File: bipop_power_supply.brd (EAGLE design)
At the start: 160 x 100 mm, 23 parts, among them IC1 LM1117MP-3.3, IC2 LM1117MP-5.0

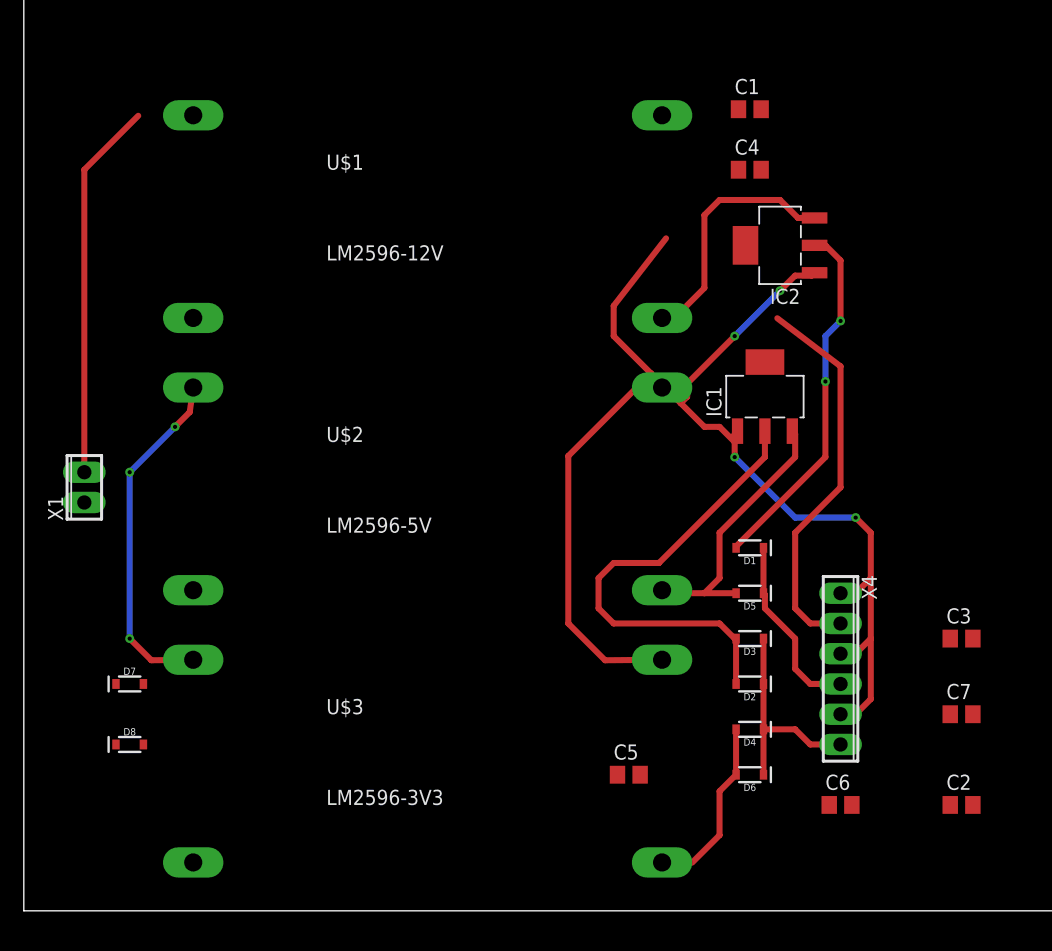
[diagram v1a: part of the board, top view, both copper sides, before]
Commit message: plytka z kondensatorami i diodami +pdfy
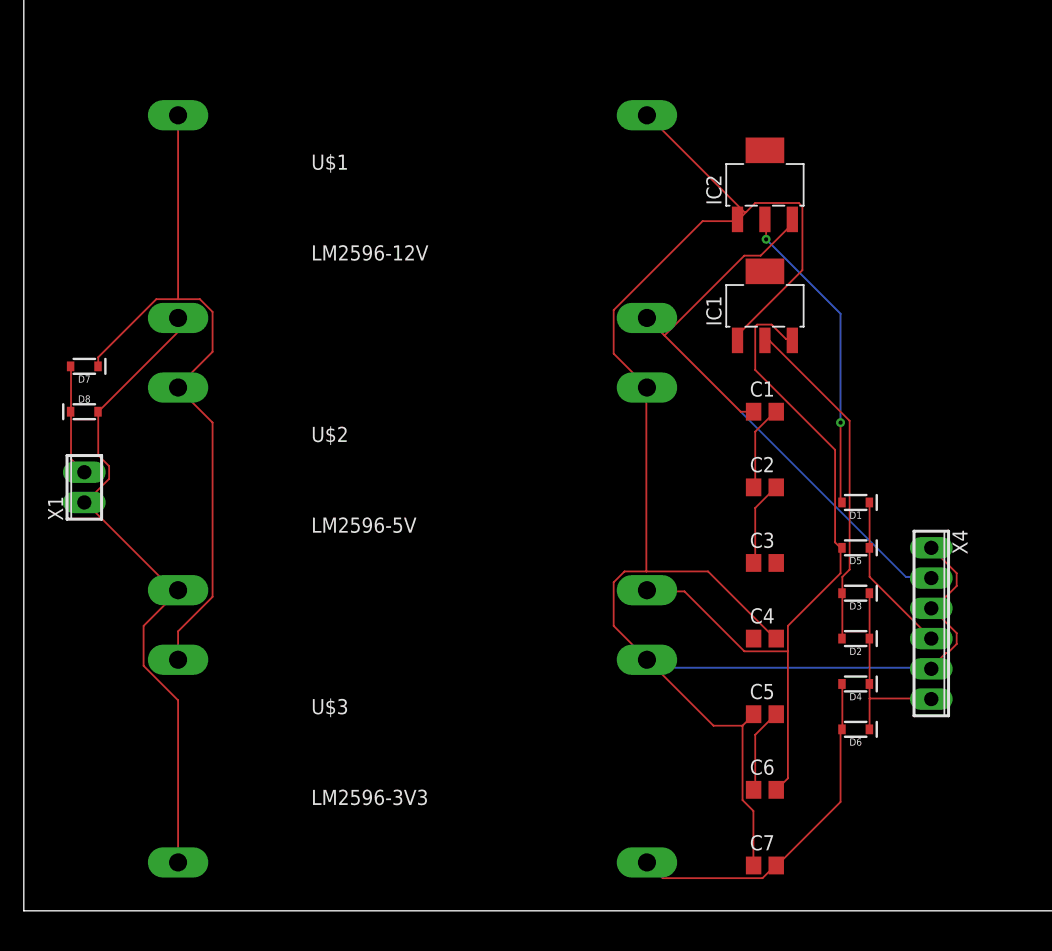
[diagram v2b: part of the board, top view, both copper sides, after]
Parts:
- moved C4 39.4 mm to (62.2, 22.9)
- moved C2 31.4 mm to (62.2, 35.6)
- moved D8 28.2 mm to (5.08, 41.9)
- moved D7 26.9 mm to (5.08, 45.7), turned to 180 degrees
- moved C1 25.4 mm to (62.2, 41.9)
- moved C7 20.8 mm to (62.2, 3.81)
- moved C3 17.7 mm to (62.2, 29.2)
- moved C5 12.5 mm to (62.2, 16.5)
- moved D3 9.67 mm to (69.8, 26.7)
- moved D4 9.67 mm to (69.8, 19.1)
- moved D6 9.67 mm to (69.8, 15.2)
- moved D1 9.67 mm to (69.8, 34.3)
- moved D2 9.67 mm to (69.8, 22.9)
- moved D5 9.67 mm to (69.8, 30.5)
- moved X4 8.52 mm to (76.2, 24.1)
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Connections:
- removed net N$10: C1.1, C4.2
- new net N$2: C2.2, C3.1
- net C12+: now also C1.1; no longer C7.1
- net GND: now also C4.2, C5.1, C7.1; no longer C2.1, C3.2, C6.1
- net N$12: now also C4.1; no longer C1.2, C3.1
- net N$4: now also C6.2; no longer C5.2
- net N$7: now also C7.2; no longer C6.2
- net N$8: now also C5.2, C6.1; no longer C2.2, C5.1
- net N$9: now also C1.2, C2.1; no longer C4.1, C7.2
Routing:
- net N$22: track 1.75 -> 55.9 mm
- net GND: track 112.5 -> 154.2 mm, vias 4 -> 0
- net N$4: track 23.4 -> 61.9 mm
- net N$17: track 29.3 -> 61.1 mm, vias 3 -> 0
- net N$1: track 31.8 -> 9.42 mm
- net N$7: track 12.7 -> 29.5 mm
- net N$5: track 40.2 -> 28.5 mm
- net N$9: track 0.00 -> 7.20 mm
- net N$8: track 0.00 -> 7.19 mm
- net N$2: track 0.00 -> 7.19 mm
- net C12+: track 53.0 -> 60.2 mm
- net N$3: track 30.5 -> 26.5 mm
- net N$16: track 15.6 -> 13.6 mm
- net N$11: track 18.4 -> 16.7 mm

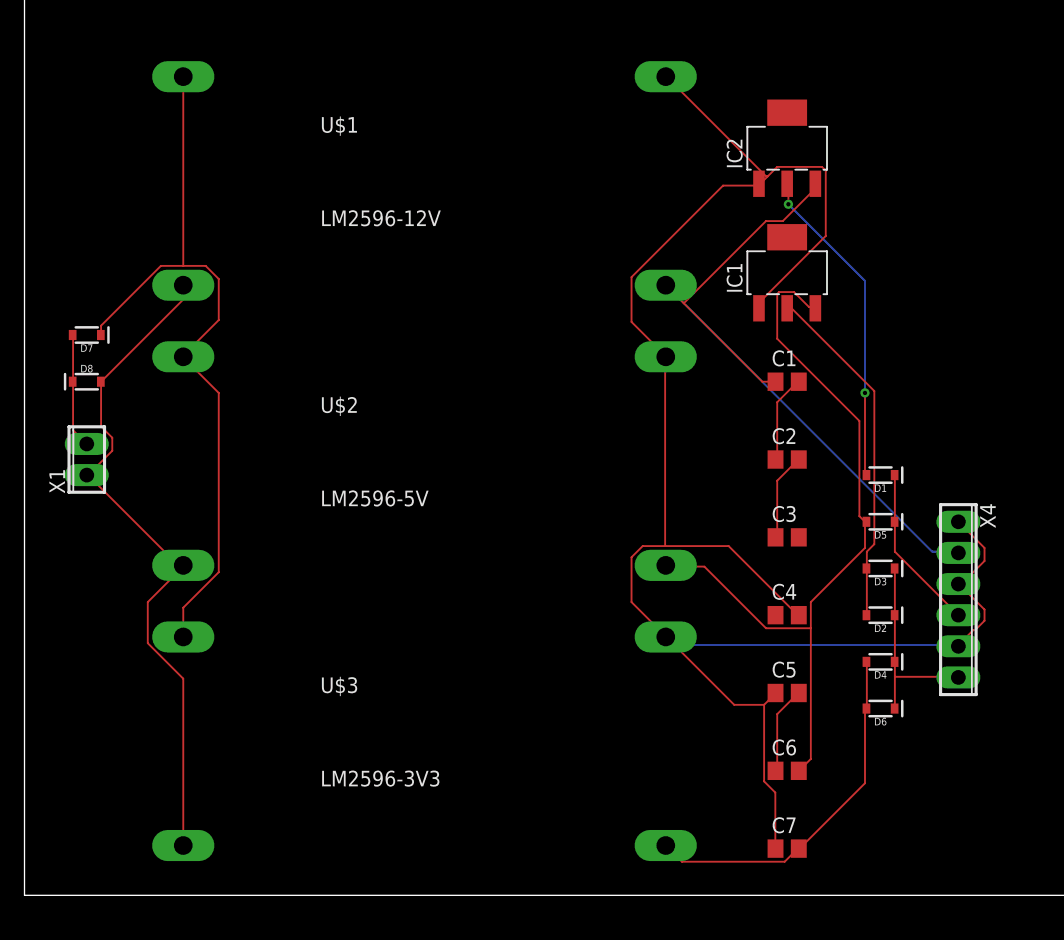
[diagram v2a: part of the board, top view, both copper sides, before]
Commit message: added diodes, capacitors
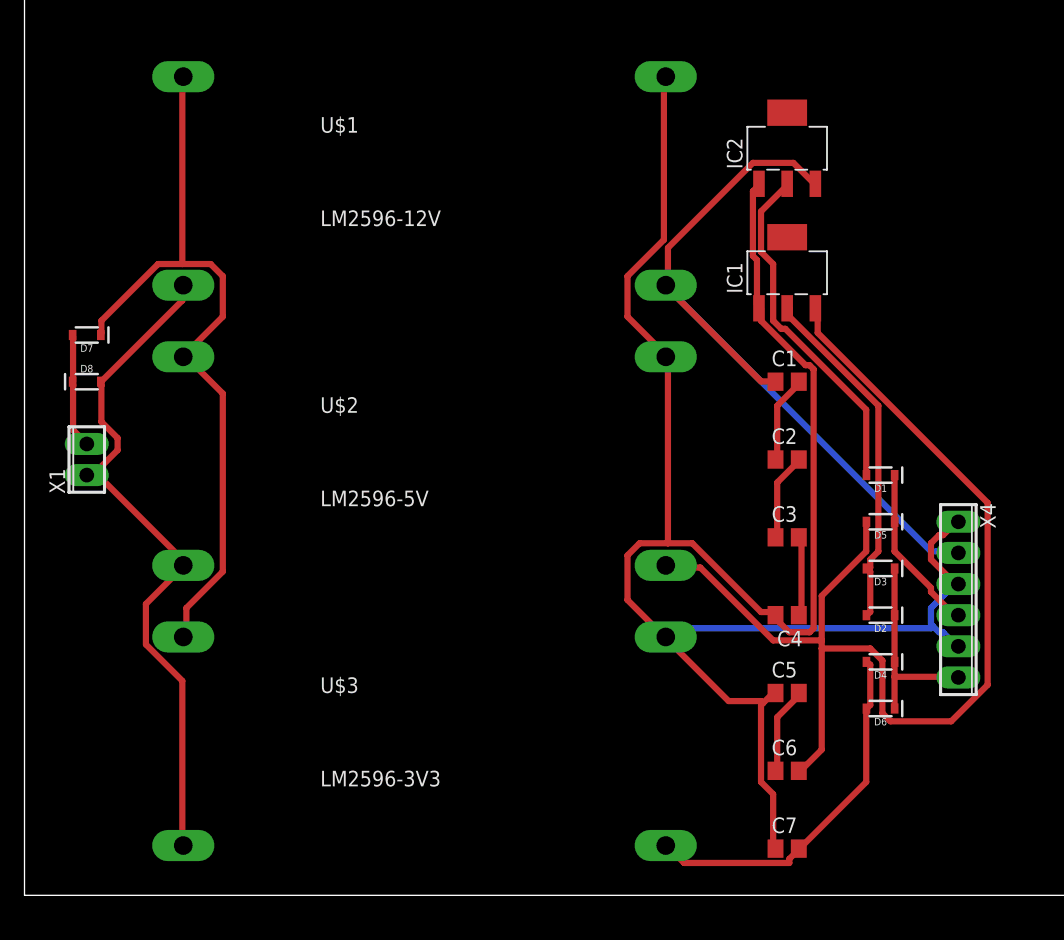
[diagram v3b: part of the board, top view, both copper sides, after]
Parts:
- turned C4 to 180 degrees
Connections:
- removed net N$12: C4.1
- new net N$6: C3.2, C4.1
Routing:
- net N$4: track 61.9 -> 94.3 mm
- net GND: track 154.2 -> 167.5 mm
- net N$6: track 0.00 -> 6.54 mm
- net C12+: track 60.2 -> 63.9 mm
- net N$3: track 26.5 -> 28.4 mm, vias 2 -> 0
- net N$17: track 61.1 -> 62.4 mm
- net N$22: track 55.9 -> 57.2 mm
- net N$5: track 28.5 -> 29.0 mm

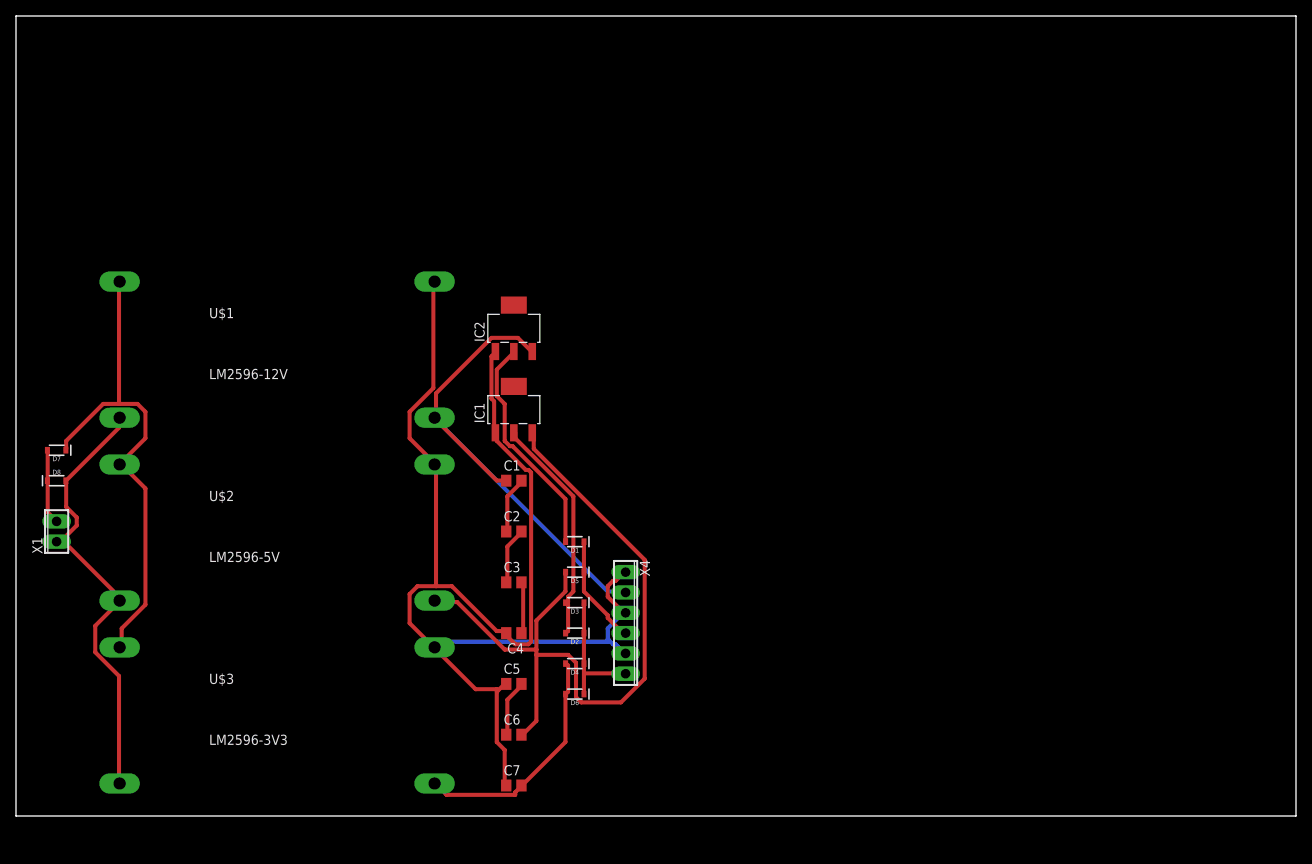
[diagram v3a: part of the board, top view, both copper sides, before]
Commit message: Changed connector in bipop_power_supply board, modified routing and board's dimensions.
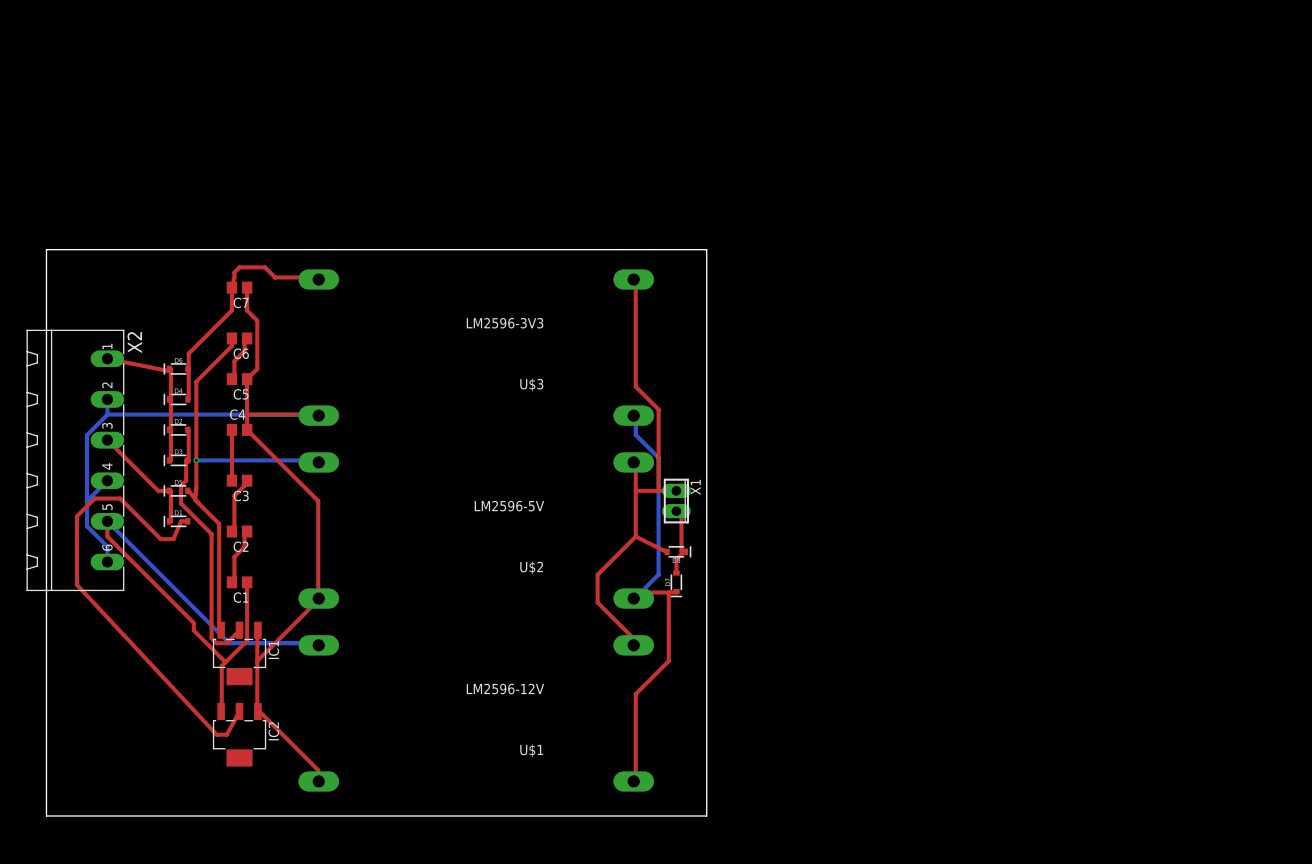
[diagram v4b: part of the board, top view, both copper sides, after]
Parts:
- removed X4: (no value), con-phoenix-254:6POL254
- added X2: MSTBA6, con-phoenix-508:MSTBA6
- moved D7 79.2 mm to (82.5, 29.2), turned to 90 degrees
- moved D8 78.0 mm to (82.5, 33.0), turned to 180 degrees
- moved X1 77.6 mm to (82.5, 39.4), turned to 270 degrees
- moved C7 71.1 mm to (27.9, 66.0), turned to 180 degrees
- moved D6 64.1 mm to (20.3, 55.9), turned to 0 degrees
- moved IC2 61.3 mm to (27.9, 10.2), turned to 180 degrees
- moved C6 60.2 mm to (27.9, 59.7), turned to 180 degrees
- moved D4 59.5 mm to (20.3, 52.1), turned to 0 degrees
- moved D2 55.7 mm to (20.3, 48.3), turned to 0 degrees
- moved U$1 52.9 mm to (58.4, 12.7), turned to 180 degrees
- moved U$3 52.9 mm to (58.4, 58.4), turned to 180 degrees
- moved D3 52.6 mm to (20.3, 44.5), turned to 0 degrees
- moved C5 51.3 mm to (27.9, 54.6), turned to 180 degrees
- moved D5 50.6 mm to (20.3, 40.6), turned to 0 degrees
- moved D1 49.6 mm to (20.3, 36.8), turned to 0 degrees
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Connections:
- net C12+: now also X2.5; no longer X4.2
- net GND: now also X2.2, X2.4, X2.6; no longer X4.1, X4.3, X4.5
- net N$11: now also X2.1; no longer X4.6
- net N$16: now also X2.3; no longer X4.4
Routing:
- net N$4: track 94.3 -> 57.3 mm, vias 0 -> 1
- net GND: track 167.5 -> 138.2 mm
- net N$3: track 28.4 -> 57.1 mm
- net C12+: track 63.9 -> 74.1 mm
- net N$22: track 57.2 -> 64.1 mm
- net N$17: track 62.4 -> 56.7 mm
- net N$5: track 29.0 -> 32.8 mm
- net N$11: track 16.6 -> 20.3 mm
- net N$8: track 7.47 -> 6.24 mm
- net N$16: track 13.8 -> 14.6 mm
- net N$1: track 9.37 -> 8.82 mm
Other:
- board size 160 x 100 mm -> 82.5 x 70.8 mm

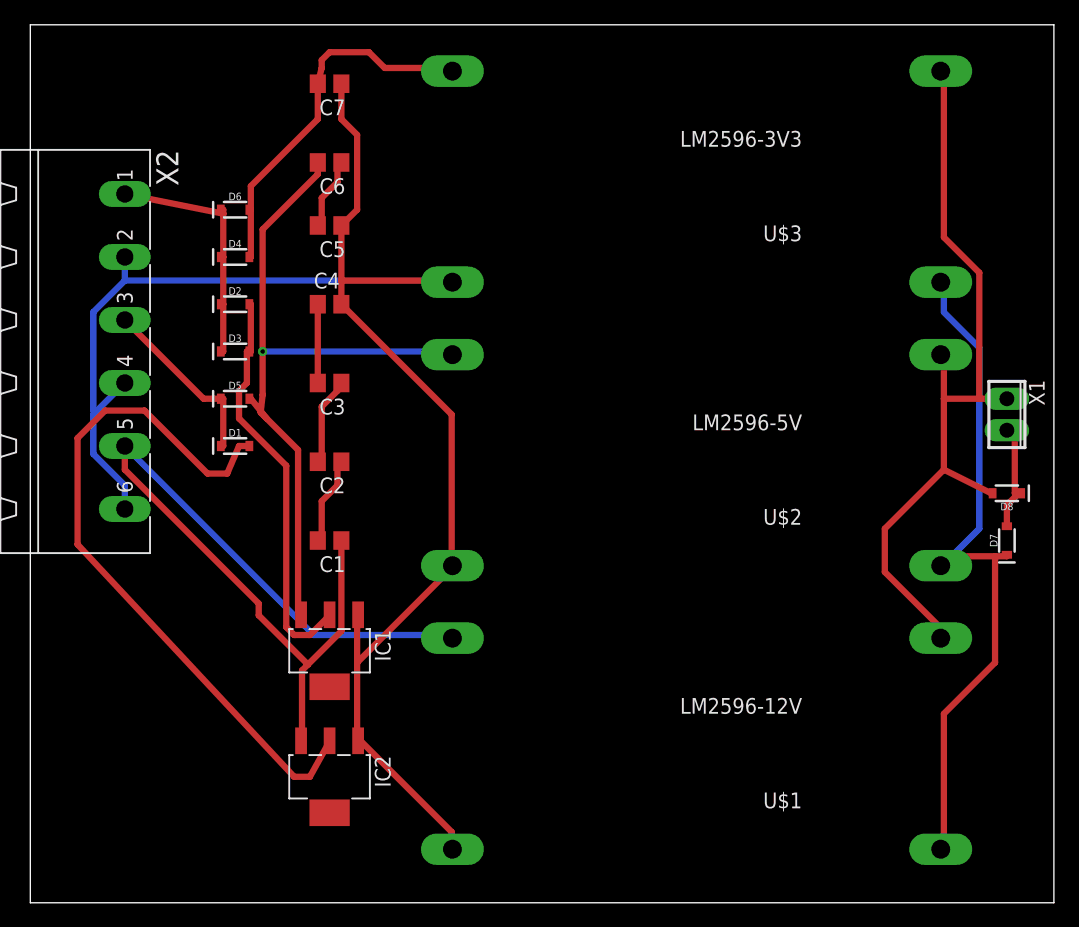
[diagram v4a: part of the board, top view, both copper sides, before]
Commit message: Fixed polarisation in power_supply board.
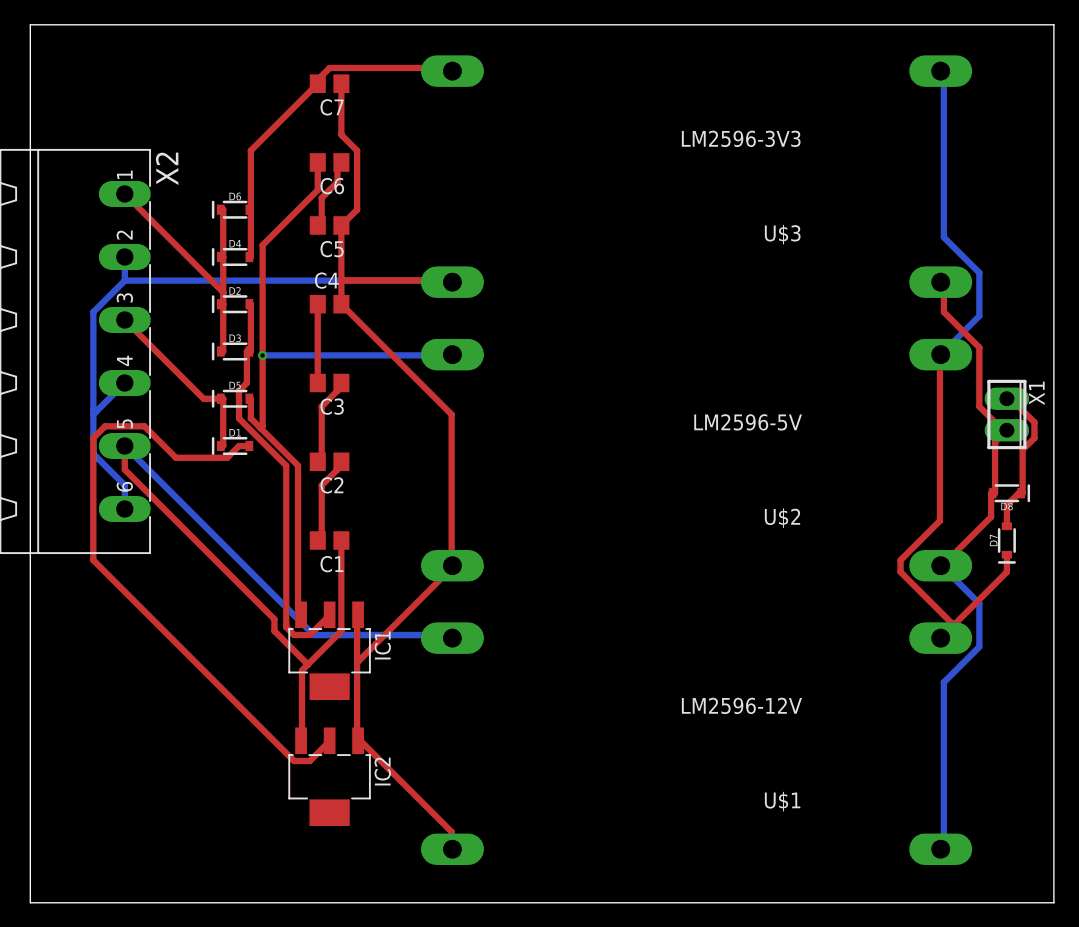
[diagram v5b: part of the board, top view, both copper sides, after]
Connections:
- removed net N$17: D7.C, U$1.V_IN-, U$2.V_IN-, U$3.V_IN-
- new net N$10: D7.A, D8.C, X1.1
- net N$1: now also D8.A, U$1.V_IN-, U$2.V_IN-, U$3.V_IN-; no longer D7.A, D8.C
- net N$22: now also D7.C; no longer D8.A, X1.1
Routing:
- net N$17: track 56.7 -> 0.00 mm
- net N$1: track 8.82 -> 53.2 mm
- net N$10: track 0.00 -> 12.5 mm
- net N$3: track 57.1 -> 50.7 mm
- net N$22: track 64.1 -> 60.7 mm
- net N$11: track 20.3 -> 23.4 mm
- net N$7: track 29.9 -> 28.4 mm
- net N$4: track 57.3 -> 57.9 mm
